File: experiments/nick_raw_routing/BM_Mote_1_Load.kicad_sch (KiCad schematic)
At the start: 9 parts, among them U11 TPS26621DRCR

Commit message: added straps
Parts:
- R34: footprint Vault:RESC1005X40X25LL05T10 -> 0402; FOOTPRINT 0402 -> (none)

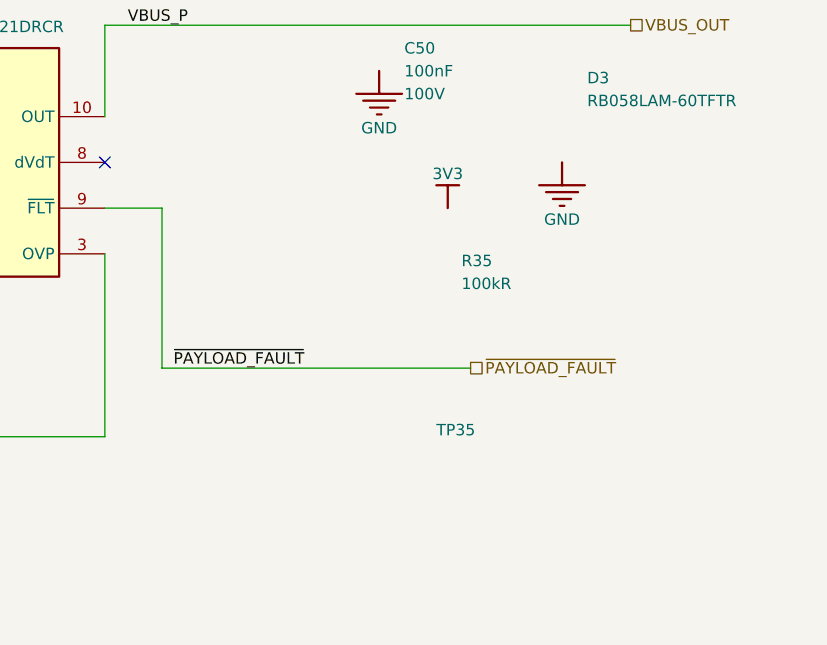
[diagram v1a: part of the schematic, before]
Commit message: Added I2C0, I2C1, I2C2 and fix to load switch
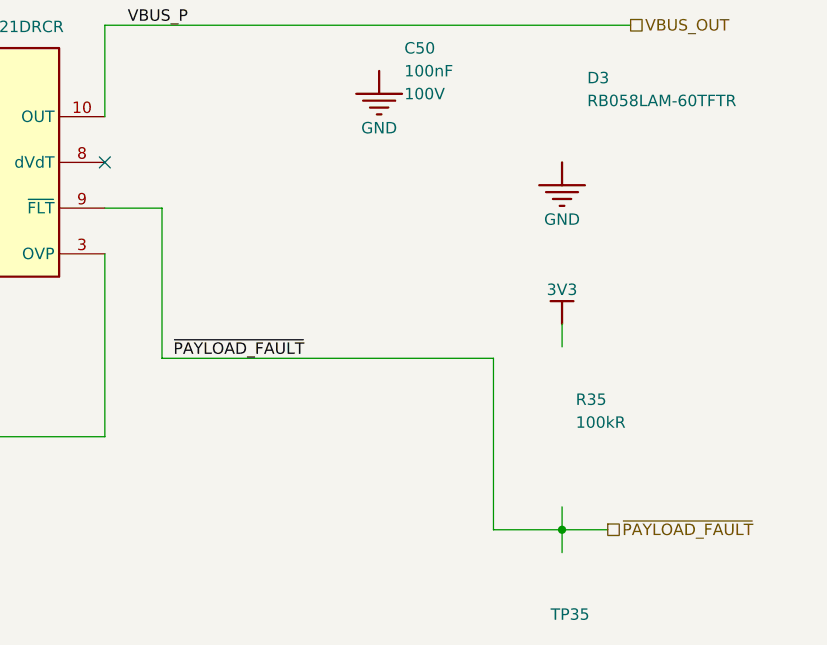
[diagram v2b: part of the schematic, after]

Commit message: Fix import connectivity
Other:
- moved on the sheet: R41

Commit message: Cleaned ERC before moving on to the Power 5V work
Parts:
- R34: footprint 0402 -> Vault:FP-RC0402-0_4-IPC_C
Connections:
- net GND: now also R34.1
- net ISET: now also R34.2
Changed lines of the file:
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@@
 		(lib_id "BM_Mote_000639-AB-altium-import:Load_1_RES_Altium Content Vault_0")
 		(at 151.13 158.75 0)
-		(unit 0)
+		(unit 1)
 		(body_style 1)
 		(exclude_from_sim no)
@@
 			)
 		)
-		(property "Footprint" "0402"
+		(property "Footprint" "Vault:FP-RC0402-0_4-IPC_C"
 			(at 152.908 150.622 0)
 			(hide yes)
@@
 				(path "/30e82bf5-1344-486b-817c-02d3b0649ce4/3c398828-e355-49f6-be37-cb3640d2c671/c7831528-f0a3-4ef0-807c-45964c3ded89"
 					(reference "R34")
-					(unit 0)
-				)
-			)
+					(unit 1)
+				)
+			)
